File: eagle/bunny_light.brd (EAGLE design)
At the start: 50 x 50 mm, 16 parts, among them IC1 ATMEGA328P_PDIP, J1 USB-B-S, U1 5V, Y1 16Mhz

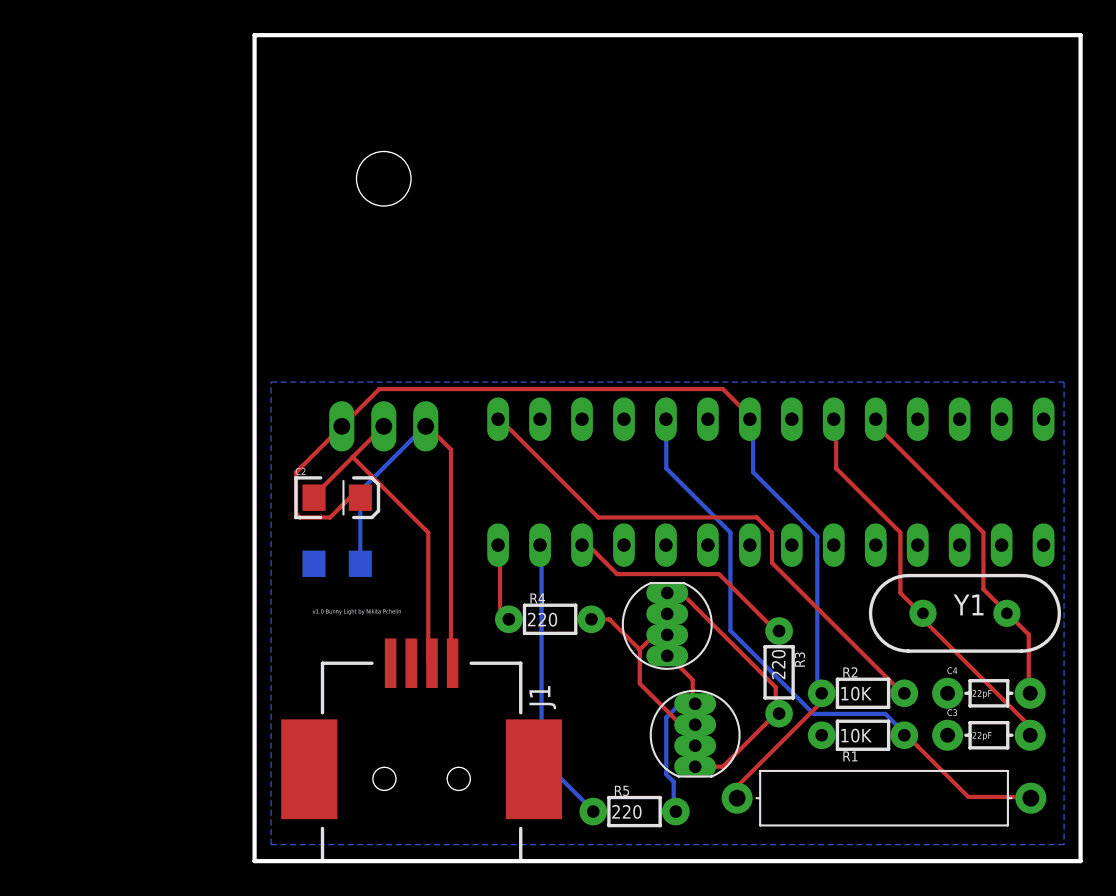
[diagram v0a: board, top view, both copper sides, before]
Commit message: Second iteration after receiving the board: 	- corrected wrong components (surface mount vs. through hole) 	- added PTC fuse 	- used larger footprints for the resistors 	- corrected RGB LEDs overlapping
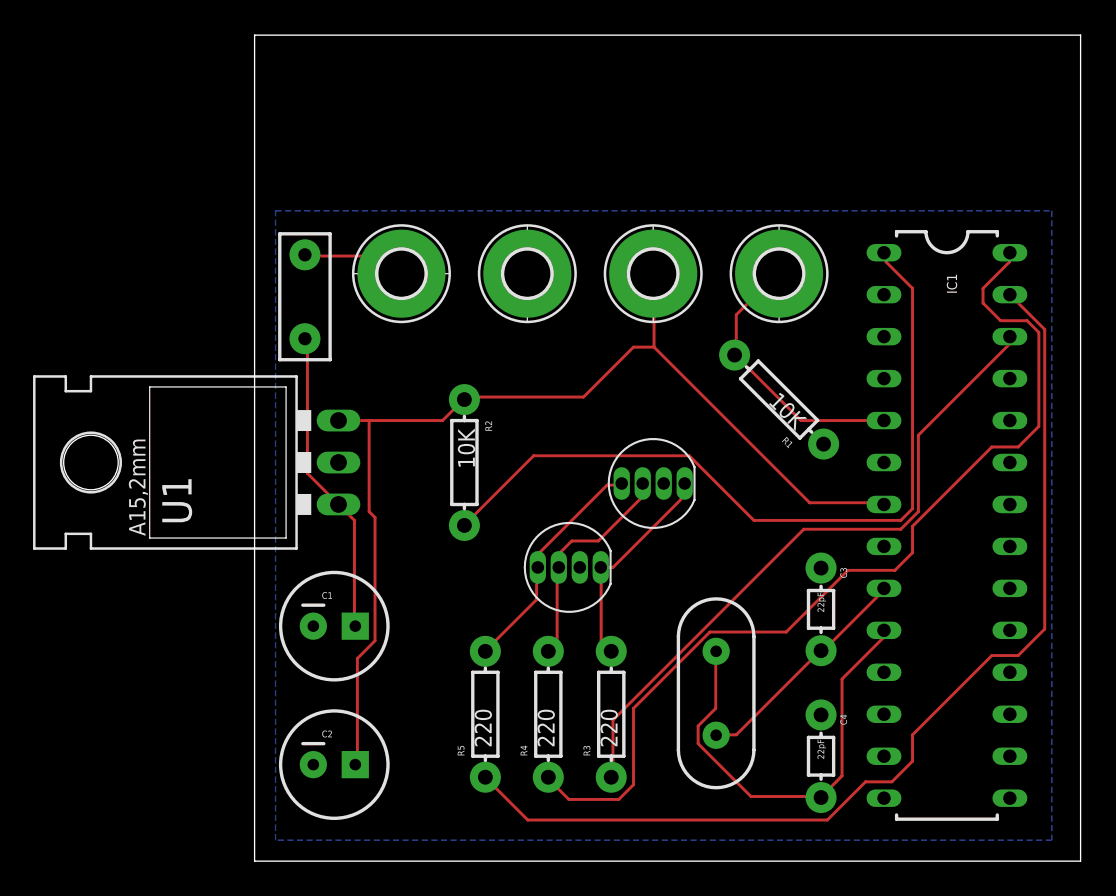
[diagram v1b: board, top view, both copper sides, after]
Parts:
- removed J1: USB-B-S, SparkFun-Connectors:USB-B-SMT
- removed S1: SWITCH, SparkFun-Electromechanical:REED_SWITCH_PLASTIC
- added H1: GND, holes:2,8-PAD
- added H2: 5V, holes:2,8-PAD
- added H3, H4: BTN, holes:2,8-PAD
- added U$1: PTCPTH, SparkFun-PowerIC:PTC
- C1, C2: device SparkFun-Capacitors:EIA3216 -> SparkFun-Capacitors:CPOL-RADIAL-100UF-25V
- R1, R2, R3, R4, R5: device SparkFun-Resistors:1/6W-RES -> SparkFun-Resistors:AXIAL-0.3EZ
- moved R2 27.9 mm to (12.7, 24.1), turned to 270 degrees
- moved R1 20.9 mm to (31.8, 27.9), turned to 135 degrees
- moved C2 16.2 mm to (4.83, 5.84)
- moved Y1 15.8 mm to (27.9, 10.2), turned to 270 degrees
- moved C3 12.7 mm to (34.3, 15.2), turned to 270 degrees
- moved D2 12.7 mm to (19.1, 17.8), turned to 0 degrees
- moved IC1 11.0 mm to (41.9, 20.3), flipped to the top, turned to 270 degrees
- moved C4 10.9 mm to (34.3, 6.35), turned to 270 degrees
- moved R5 10.8 mm to (14.0, 8.89), turned to 90 degrees
- moved R3 10.5 mm to (21.6, 8.89), turned to 90 degrees
- moved U1 8.88 mm to (1.27, 24.1), flipped to the top, turned to 90 degrees
- moved D1 8.57 mm to (24.1, 22.9), turned to 0 degrees
- moved R4 5.75 mm to (17.8, 8.89), turned to 90 degrees
- moved C1 3.78 mm to (4.83, 14.2), flipped to the top, turned to 0 degrees
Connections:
- new net N$12: H2.B2,8, U$1.P$1
- net 5V: now also C2.1, H3.B2,8, R2.P$1; no longer C2.A, R2.1, S1.P$1
- net GND: now also C1.2, C2.2, H1.B2,8, R1.P$1; no longer C1.C, C2.C, J1.GND, R1.1
- net N$1: now also C1.1, U$1.P$2; no longer C1.A, J1.VUSB
- net N$10: now also R4.P$1; no longer R4.1
- net N$11: now also R5.P$1; no longer R5.1
- net N$4: now also R2.P$2; no longer R2.2
- net N$5: now also H4.B2,8, R1.P$2; no longer R1.2, S1.P$2
- net N$6: now also R3.P$2; no longer R3.2
- net N$7: now also R4.P$2; no longer R4.2
- net N$8: now also R5.P$2; no longer R5.2
- net N$9: now also R3.P$1; no longer R3.1
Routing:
- net N$10: track 4.73 -> 56.8 mm
- net N$11: track 17.4 -> 61.8 mm
- net N$9: track 14.1 -> 40.1 mm
- net GND: track 20.6 -> 0.00 mm
- net N$5: track 36.9 -> 16.8 mm
- net N$4: track 32.7 -> 47.1 mm
- net N$2: track 24.4 -> 14.0 mm
- net N$1: track 25.0 -> 18.7 mm
- net N$12: track 0.00 -> 6.30 mm
- net N$3: track 20.5 -> 26.5 mm
- net N$6: track 17.0 -> 12.9 mm
- net N$8: track 11.7 -> 14.2 mm
- net N$7: track 12.2 -> 13.6 mm
- net 5V: track 64.3 -> 64.9 mm
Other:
- board text added: "5V"
- board text added: "BTN"
- board text added: "BunnyLight v1.1"
- board text added: "C"
- board text added: "GND"
- board text removed: "v1.0 Bunny Light by Nikita Pchelin"
